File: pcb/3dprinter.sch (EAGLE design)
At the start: 1 part

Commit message: Footprint of TMC2100 and reference schematic added
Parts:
- added C1, C2, C4, C5, C6: 100n, 3dprinter:C-EUC0603
- added C3: 1u, 3dprinter:C-EUC0603
- added C7: 470n, 3dprinter:C-EUC0603
- added C8: 4.7u, 3dprinter:C-EUC0603
- added IC1: TMC2100, 3dprinter:TMC2100
- added PI_HEADER: (no value), 3dprinter:MA20-2
- added R1, R2: TBD, 3dprinter:R-US_R0805
- added R3: TBD, 3dprinter:R-US_R0603
- added R4: 2R2 / 3R3, 3dprinter:R-US_R0603
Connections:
- new net +12V: C1.2, C2.2, C3.2, C4.2, IC1.VS, IC1.VSA
- new net +5V: C6.1, IC1.VCC_IO
- new net 5V_M1: C8.1, IC1.5VOUT, R3.2, R4.2
- new net BRA_M1: IC1.BRA, R2.2
- new net BRB_M1: IC1.BRB, R1.2
- new net CFG1_M1: IC1.CFG1
- new net CFG2_M1: IC1.CFG2
- new net CPI_M1: C5.1, IC1.CPI
- new net CPO_M1: C5.2, IC1.CPO
- new net DIR_M1: IC1.DIR
- new net EN_M1: IC1.CFG6_!ENABLE
- new net GND: C1.1, C2.1, C3.1, C6.2, C7.2, C8.2, IC1.CFG0, IC1.CLK, IC1.GNDA, IC1.GNDD, IC1.GNDP, IC1.N.C, IC1.PAD, IC1.TST_MODE, R1.1, R2.1
- new net IREF_M1: IC1.AIN_IREF, R3.1
- new net OA1_M1: IC1.OA1
- new net OA2_M1: IC1.OA2
- new net OB1_M1: IC1.OB1
- new net OB2_M1: IC1.OB2
- new net PI_3V31: PI_HEADER.1
- new net STEP_M1: IC1.STEP
- new net VCC_M1: C7.1, IC1.VCC, R4.1
- new net VCP_M1: C4.1, IC1.VCP
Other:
- note added: "Raspberry Pi Header"
- note added: "TESTPOINT HERE"
- note added: "TODO: Trimpot Calculate I sense calculations Thermal pad on BOT? CFG table in schematic"
- note added: "TRIMPOT HERE"

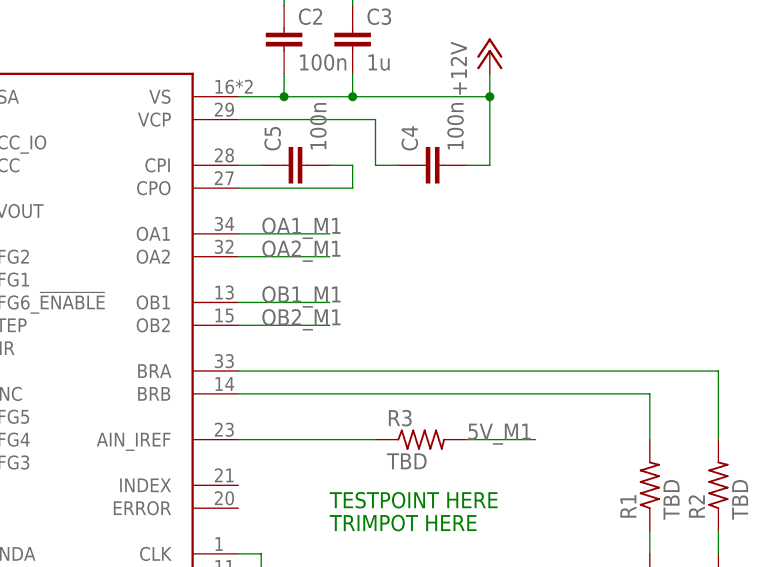
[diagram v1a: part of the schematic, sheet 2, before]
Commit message: TMC2100 initial routing
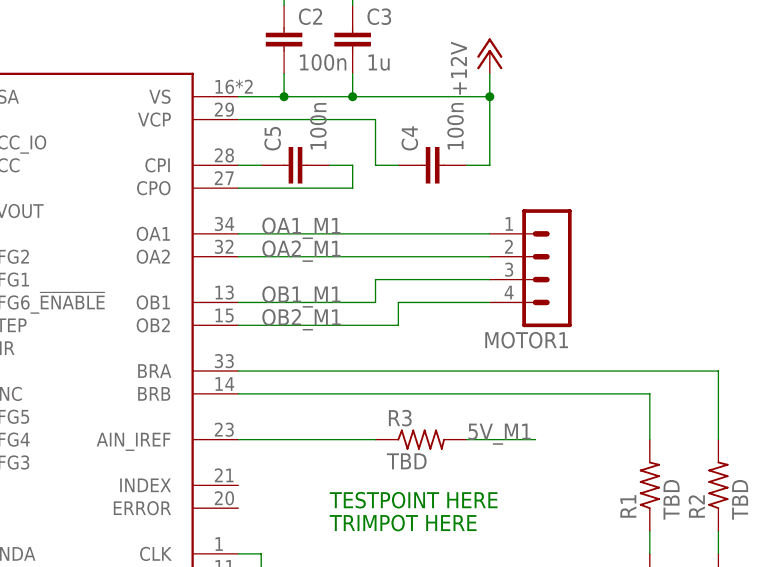
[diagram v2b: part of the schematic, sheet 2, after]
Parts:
- added MOTOR1: (no value), 3dprinter:MA04-1
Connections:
- net OA1_M1: now also MOTOR1.1
- net OA2_M1: now also MOTOR1.2
- net OB1_M1: now also MOTOR1.3
- net OB2_M1: now also MOTOR1.4
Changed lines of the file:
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@@
 <setting verticaltext="up"/>
 </settings>
-<grid distance="0.1" unitdist="inch" unit="inch" style="lines" multiple="1" display="yes" altdistance="0.01" altunitdist="inch" altunit="inch"/>
+<grid distance="0.1" unitdist="inch" unit="inch" style="lines" multiple="1" display="no" altdistance="0.01" altunitdist="inch" altunit="inch"/>
 <layers>
 <layer number="1" name="Top" color="4" fill="1" visible="no" active="no"/>
@@
 <part name="C8" library="3dprinter" deviceset="C-EU" device="C0603" value="4.7u"/>
 <part name="COPå8" library="supply" deviceset="GND" device=""/>
+<part name="MOTOR1" library="3dprinter" deviceset="MA04-1" device=""/>
 </parts>
 <sheets>
@@
 <instance part="C8" gate="G$1" x="45.72" y="208.28"/>
 <instance part="COPå8" gate="1" x="45.72" y="198.12"/>
+<instance part="MOTOR1" gate="1" x="139.7" y="205.74" rot="R180"/>
 </instances>
 <busses>
@@
 <segment>
 <pinref part="IC1" gate="G$1" pin="OA1"/>
-<wire x1="104.14" y1="210.82" x2="114.3" y2="210.82" width="0.1524" layer="91"/>
 <label x="106.68" y="210.82" size="1.778" layer="95"/>
+<wire x1="104.14" y1="210.82" x2="132.08" y2="210.82" width="0.1524" layer="91"/>
+<pinref part="MOTOR1" gate="1" pin="1"/>
 </segment>
 </net>
@@
 <segment>
 <pinref part="IC1" gate="G$1" pin="OA2"/>
-<wire x1="104.14" y1="208.28" x2="114.3" y2="208.28" width="0.1524" layer="91"/>
 <label x="106.68" y="208.28" size="1.778" layer="95"/>
+<wire x1="104.14" y1="208.28" x2="132.08" y2="208.28" width="0.1524" layer="91"/>
+<pinref part="MOTOR1" gate="1" pin="2"/>
 </segment>
 </net>
@@
 <segment>
 <pinref part="IC1" gate="G$1" pin="OB1"/>
-<wire x1="104.14" y1="203.2" x2="114.3" y2="203.2" width="0.1524" layer="91"/>
+<wire x1="104.14" y1="203.2" x2="119.38" y2="203.2" width="0.1524" layer="91"/>
 <label x="106.68" y="203.2" size="1.778" layer="95"/>
+<wire x1="119.38" y1="203.2" x2="119.38" y2="205.74" width="0.1524" layer="91"/>
+<wire x1="119.38" y1="205.74" x2="132.08" y2="205.74" width="0.1524" layer="91"/>
+<pinref part="MOTOR1" gate="1" pin="3"/>
 </segment>
 </net>
@@
 <segment>
 <pinref part="IC1" gate="G$1" pin="OB2"/>
-<wire x1="104.14" y1="200.66" x2="114.3" y2="200.66" width="0.1524" layer="91"/>
+<wire x1="104.14" y1="200.66" x2="121.92" y2="200.66" width="0.1524" layer="91"/>
 <label x="106.68" y="200.66" size="1.778" layer="95"/>
-</segment>
-</net>
+<wire x1="121.92" y1="200.66" x2="121.92" y2="203.2" width="0.1524" layer="91"/>
+<wire x1="121.92" y1="203.2" x2="132.08" y2="203.2" width="0.1524" layer="91"/>
+<pinref part="MOTOR1" gate="1" pin="4"/>
+</segment>
+</net>

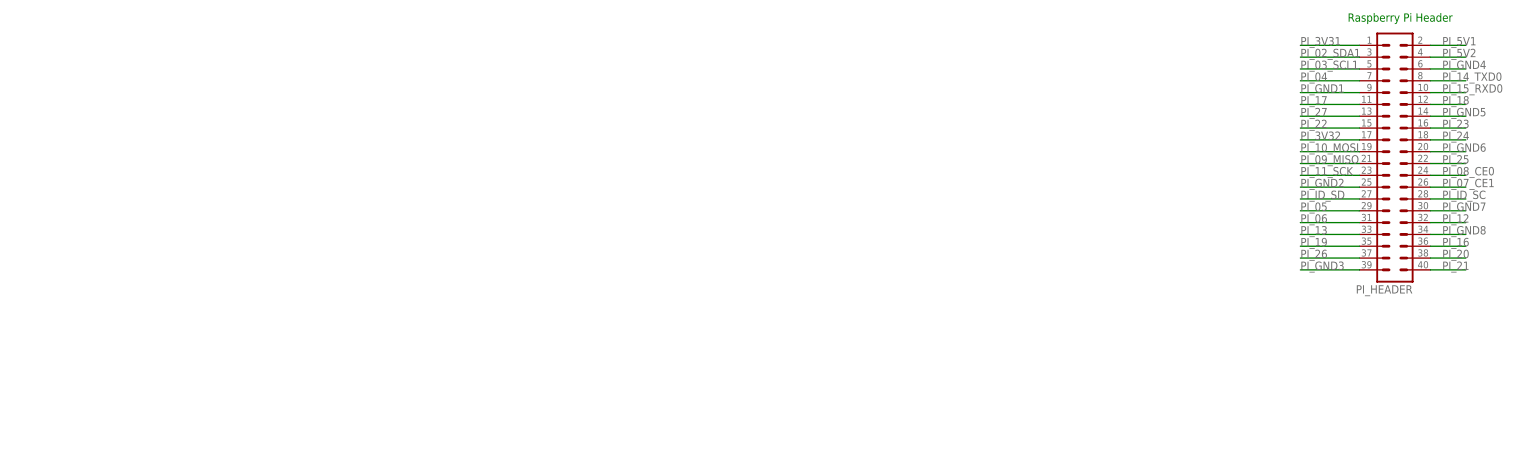
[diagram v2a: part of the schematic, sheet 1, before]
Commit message: Added NRF51822 footprint
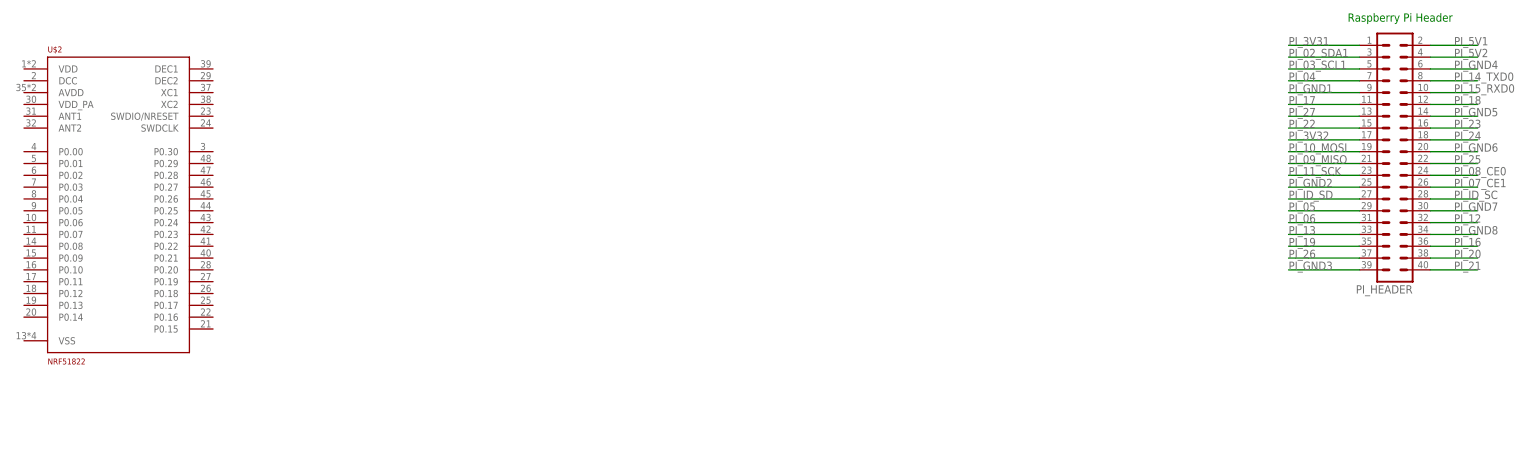
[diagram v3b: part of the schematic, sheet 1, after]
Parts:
- added U$2: NRF51822, 3dprinter:NRF51822
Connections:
- new net PI_02_SDA1: PI_HEADER.3
- new net PI_03_SCL1: PI_HEADER.5
- new net PI_04: PI_HEADER.7
- new net PI_05: PI_HEADER.29
- new net PI_06: PI_HEADER.31
- new net PI_07_CE1: PI_HEADER.26
- new net PI_08_CE0: PI_HEADER.24
- new net PI_09_MISO: PI_HEADER.21
- new net PI_10_MOSI: PI_HEADER.19
- new net PI_11_SCK: PI_HEADER.23
- new net PI_12: PI_HEADER.32
- new net PI_13: PI_HEADER.33
- new net PI_14_TXD0: PI_HEADER.8
- new net PI_15_RXD0: PI_HEADER.10
- new net PI_16: PI_HEADER.36
- new net PI_17: PI_HEADER.11
- new net PI_18: PI_HEADER.12
- new net PI_19: PI_HEADER.35
- new net PI_20: PI_HEADER.38
- new net PI_21: PI_HEADER.40
- new net PI_22: PI_HEADER.15
- new net PI_23: PI_HEADER.16
- new net PI_24: PI_HEADER.18
- new net PI_25: PI_HEADER.22
- new net PI_26: PI_HEADER.37
- new net PI_27: PI_HEADER.13
- new net PI_3V32: PI_HEADER.17
- new net PI_5V1: PI_HEADER.2
- new net PI_5V2: PI_HEADER.4
- new net PI_GND1: PI_HEADER.9
- new net PI_GND2: PI_HEADER.25
- new net PI_GND3: PI_HEADER.39
- new net PI_GND4: PI_HEADER.6
- new net PI_GND5: PI_HEADER.14
- new net PI_GND6: PI_HEADER.20
- new net PI_GND7: PI_HEADER.30
- new net PI_GND8: PI_HEADER.34
- new net PI_ID_SC: PI_HEADER.28
- new net PI_ID_SD: PI_HEADER.27
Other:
- moved on the sheet: IC1

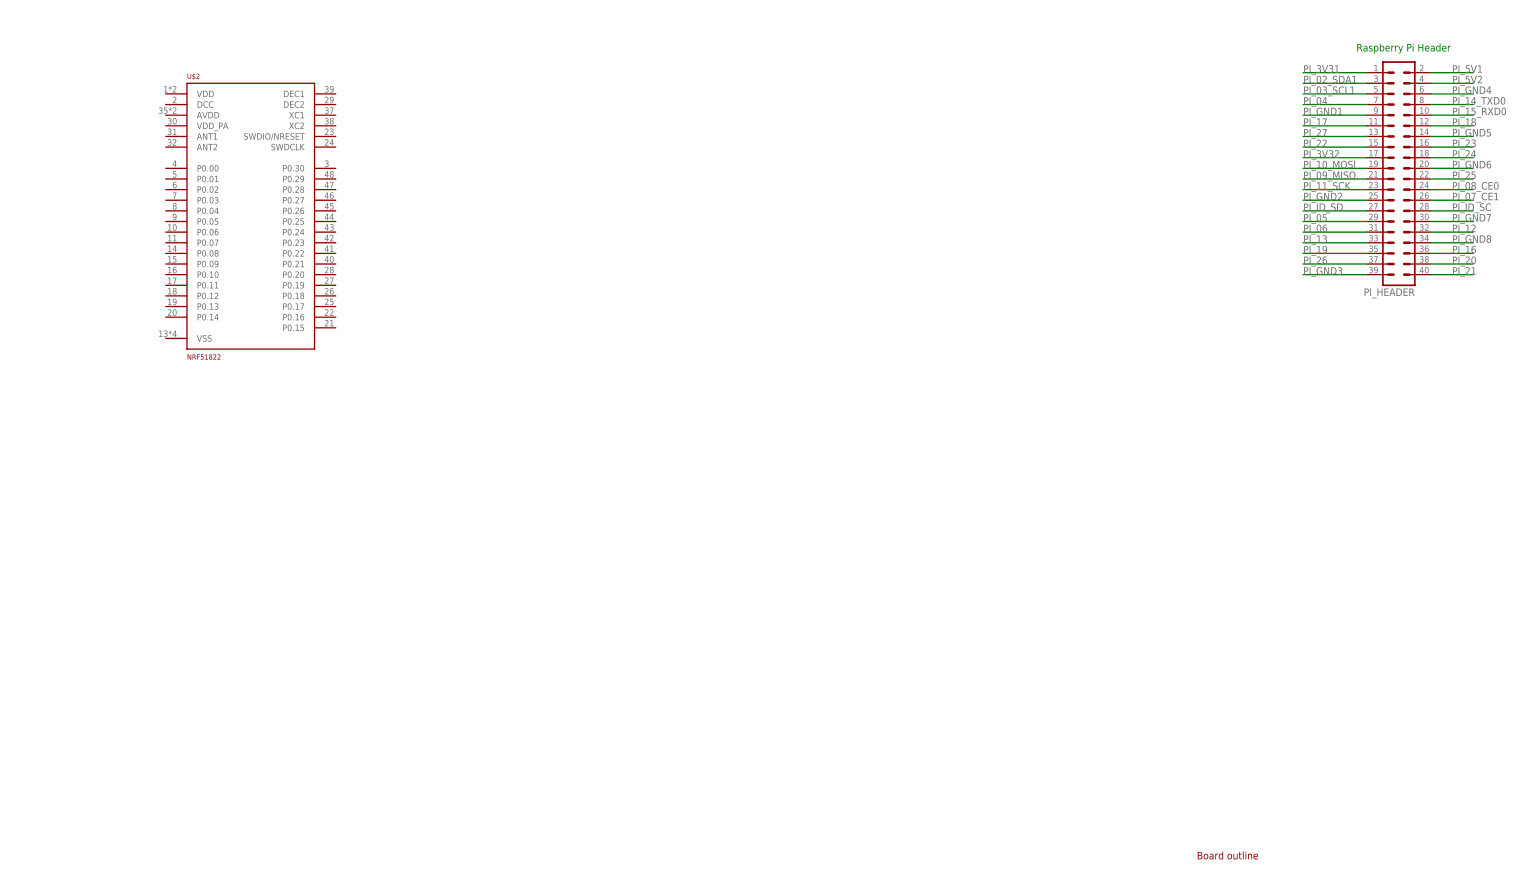
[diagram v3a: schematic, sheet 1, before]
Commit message: Example circuit nrf51 passives
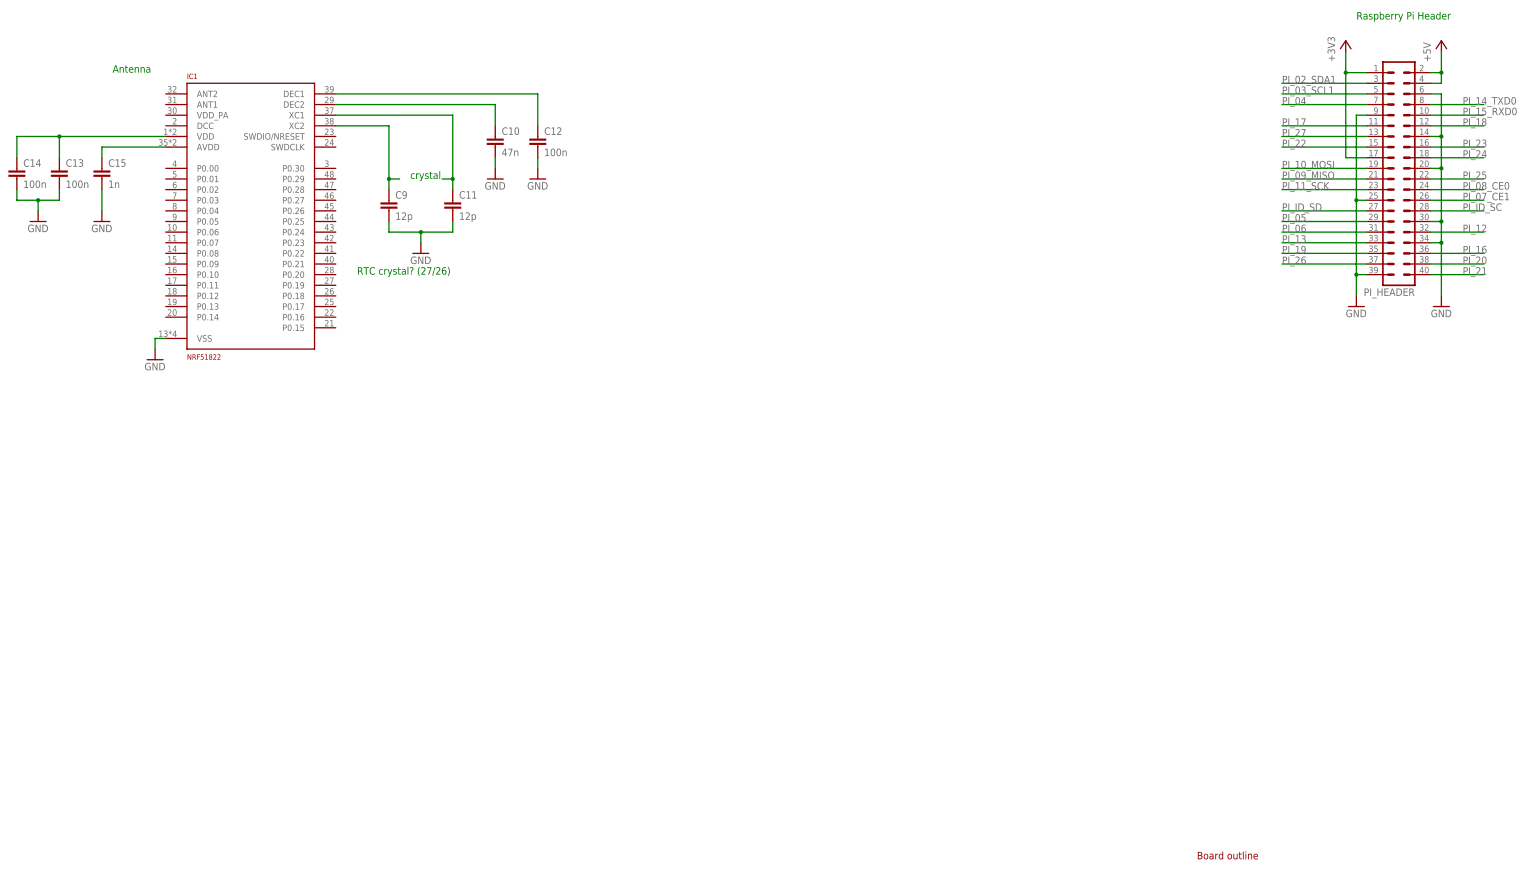
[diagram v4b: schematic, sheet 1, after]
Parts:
- removed U$2: NRF51822, 3dprinter:NRF51822
- added C10: 47n, 3dprinter:C-EUC0603
- added C11, C9: 12p, 3dprinter:C-EUC0603
- added C12, C13, C14: 100n, 3dprinter:C-EUC0603
- added C15: 1n, 3dprinter:C-EUC0603
- added IC2: TMC2100, 3dprinter:TMC2100
- IC1: value TMC2100 -> NRF51822; device 3dprinter:TMC2100 -> 3dprinter:NRF51822
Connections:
- removed net PI_3V31: PI_HEADER.1
- removed net PI_3V32: PI_HEADER.17
- removed net PI_5V1: PI_HEADER.2
- removed net PI_5V2: PI_HEADER.4
- removed net PI_GND1: PI_HEADER.9
- removed net PI_GND2: PI_HEADER.25
- removed net PI_GND3: PI_HEADER.39
- removed net PI_GND4: PI_HEADER.6
- removed net PI_GND5: PI_HEADER.14
- removed net PI_GND6: PI_HEADER.20
- removed net PI_GND7: PI_HEADER.30
- removed net PI_GND8: PI_HEADER.34
- new net +3V3: PI_HEADER.1, PI_HEADER.17
- new net N$1: C9.1, IC1.XC2
- new net N$2: C11.1, IC1.XC1
- new net N$3: C12.1, IC1.DEC1
- new net N$4: C10.1, IC1.DEC2
- new net N$5: C13.1, C14.1, IC1.VDD
- new net N$6: C15.1, IC1.AVDD
- net +12V: now also IC2.VS, IC2.VSA; no longer IC1.VS, IC1.VSA
- net +5V: now also IC2.VCC_IO, PI_HEADER.2, PI_HEADER.4; no longer IC1.VCC_IO
- net 5V_M1: now also IC2.5VOUT; no longer IC1.5VOUT
- net BRA_M1: now also IC2.BRA; no longer IC1.BRA
- net BRB_M1: now also IC2.BRB; no longer IC1.BRB
- net CFG1_M1: now also IC2.CFG1; no longer IC1.CFG1
- net CFG2_M1: now also IC2.CFG2; no longer IC1.CFG2
- net CPI_M1: now also IC2.CPI; no longer IC1.CPI
- net CPO_M1: now also IC2.CPO; no longer IC1.CPO
- net DIR_M1: now also IC2.DIR; no longer IC1.DIR
- net EN_M1: now also IC2.CFG6_!ENABLE; no longer IC1.CFG6_!ENABLE
- net GND: now also C10.2, C11.2, C12.2, C13.2, C14.2, C15.2, C9.2, IC1.VSS, IC2.CFG0, IC2.CLK, IC2.GNDA, IC2.GNDD, IC2.GNDP, IC2.N.C, IC2.PAD, IC2.TST_MODE, PI_HEADER.14, PI_HEADER.20, PI_HEADER.25, PI_HEADER.30, PI_HEADER.34, PI_HEADER.39, PI_HEADER.6, PI_HEADER.9; no longer IC1.CFG0, IC1.CLK, IC1.GNDA, IC1.GNDD, IC1.GNDP, IC1.N.C, IC1.PAD, IC1.TST_MODE
- net IREF_M1: now also IC2.AIN_IREF; no longer IC1.AIN_IREF
- net OA1_M1: now also IC2.OA1; no longer IC1.OA1
- net OA2_M1: now also IC2.OA2; no longer IC1.OA2
- net OB1_M1: now also IC2.OB1; no longer IC1.OB1
- net OB2_M1: now also IC2.OB2; no longer IC1.OB2
- net STEP_M1: now also IC2.STEP; no longer IC1.STEP
- net VCC_M1: now also IC2.VCC; no longer IC1.VCC
- net VCP_M1: now also IC2.VCP; no longer IC1.VCP
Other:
- note added: "Antenna"
- note added: "RTC crystal? (27/26)"
- note added: "crystal"

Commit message: Multiplied motor driver circuit and added mosfets
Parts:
- added ANT: ANTENNA, 3dprinter:ANTENNA
- added BAL: BALUNBALUN, 3dprinter:BALUNBALUN
- added C1_M1, C1_M2, C1_M3, C1_M4, C2_M2, C2_M3, C2_M4, C4_M2, C4_M3, C4_M4, C5_M2, C5_M3, C5_M4, C6_M2, C6_M3, C6_M4: 100n, 3dprinter:C-EUC0603
- added C3_M2, C3_M3, C3_M4: 1u, 3dprinter:C-EUC0603
- added C7_M2, C7_M3, C7_M4: 470n, 3dprinter:C-EUC0603
- added C8_M2, C8_M3, C8_M4: 4.7u, 3dprinter:C-EUC0603
- added IC_M2, IC_M3, IC_M4: TMC2100, 3dprinter:TMC2100
- added MOTOR2, MOTOR3, MOTOR4, SWD: (no value), 3dprinter:MA04-1
- added POT_M1, POT_M2, POT_M3, POT_M4: TRIMPOT, 3dprinter:TRIMPOT
- added Q1, Q2, Q3, Q4: MOSFET, 3dprinter:MOSFET
- added R1_M2, R1_M3, R1_M4: 20k, 3dprinter:R-US_R0603
- added R2_M2, R2_M3, R2_M4, R3_M2, R3_M3, R3_M4: TBD, 3dprinter:R-US_R0805
- added R4_M2, R4_M3, R4_M4: 2R2 / 3R3, 3dprinter:R-US_R0603
- added Y1: CRYSTAL, 3dprinter:CRYSTAL
- C1: value 100n -> 2.2n
- R1_M1: value TBD -> 20k
- renumbered C2 to C2_M1, C3 to C3_M1, C4 to C4_M1, C5 to C5_M1, C6 to C6_M1, C7 to C7_M1, C8 to C8_M1, IC2 to IC_M1, R1 to R2_M1, R2 to R3_M1, R3 to R1_M1, R4 to R4_M1, U$1 to OUTLINE
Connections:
- removed net IREF_M1: IC_M1.AIN_IREF, R1_M1.1
- new net 5V_M2: C8_M2.1, IC_M2.5VOUT, R1_M2.2, R4_M2.2
- new net 5V_M3: C8_M3.1, IC_M3.5VOUT, R1_M3.2, R4_M3.2
- new net 5V_M4: C8_M4.1, IC_M4.5VOUT, R1_M4.2, R4_M4.2
- new net AIN_M1: IC_M1.AIN_IREF, POT_M1.2
- new net AIN_M2: IC_M2.AIN_IREF, POT_M2.2
- new net AIN_M3: IC_M3.AIN_IREF, POT_M3.2
- new net AIN_M4: IC_M4.AIN_IREF, POT_M4.2
- new net BRA_M2: IC_M2.BRA, R3_M2.2
- new net BRA_M3: IC_M3.BRA, R3_M3.2
- new net BRA_M4: IC_M4.BRA, R3_M4.2
- new net BRB_M2: IC_M2.BRB, R2_M2.2
- new net BRB_M3: IC_M3.BRB, R2_M3.2
- new net BRB_M4: IC_M4.BRB, R2_M4.2
- new net CFG1_M2: IC_M2.CFG1
- new net CFG1_M3: IC_M3.CFG1
- new net CFG1_M4: IC_M4.CFG1
- new net CFG2_M2: IC_M2.CFG2
- new net CFG2_M3: IC_M3.CFG2
- new net CFG2_M4: IC_M4.CFG2
- new net CPI_M2: C5_M2.1, IC_M2.CPI
- new net CPI_M3: C5_M3.1, IC_M3.CPI
- new net CPI_M4: C5_M4.1, IC_M4.CPI
- new net CPO_M2: C5_M2.2, IC_M2.CPO
- new net CPO_M3: C5_M3.2, IC_M3.CPO
- new net CPO_M4: C5_M4.2, IC_M4.CPO
- new net DIR_M2: IC_M2.DIR
- new net DIR_M3: IC_M3.DIR
- new net DIR_M4: IC_M4.DIR
- new net EN_M2: IC_M2.CFG6_!ENABLE
- new net EN_M3: IC_M3.CFG6_!ENABLE
- new net EN_M4: IC_M4.CFG6_!ENABLE
- new net N$10: BAL.BAL2, IC1.ANT2
- new net N$7: ANT.1, BAL.UBAL
- new net N$8: BAL.DC, C1.1, IC1.VDD_PA
- new net N$9: BAL.BAL1, IC1.ANT1
- new net OA1_M2: IC_M2.OA1, MOTOR2.1
- new net OA1_M3: IC_M3.OA1, MOTOR3.1
- new net OA1_M4: IC_M4.OA1, MOTOR4.1
- new net OA2_M2: IC_M2.OA2, MOTOR2.2
- new net OA2_M3: IC_M3.OA2, MOTOR3.2
- new net OA2_M4: IC_M4.OA2, MOTOR4.2
- new net OB1_M2: IC_M2.OB1, MOTOR2.3
- new net OB1_M3: IC_M3.OB1, MOTOR3.3
- new net OB1_M4: IC_M4.OB1, MOTOR4.3
- new net OB2_M2: IC_M2.OB2, MOTOR2.4
- new net OB2_M3: IC_M3.OB2, MOTOR3.4
- new net OB2_M4: IC_M4.OB2, MOTOR4.4
- new net POT_M1: POT_M1.1, R1_M1.1
- new net POT_M2: POT_M2.1, R1_M2.1
- new net POT_M3: POT_M3.1, R1_M3.1
- new net POT_M4: POT_M4.1, R1_M4.1
- new net STEP_M2: IC_M2.STEP
- new net STEP_M3: IC_M3.STEP
- new net STEP_M4: IC_M4.STEP
- new net SWDCLK: IC1.SWDCLK, SWD.2
- new net SWDIO: IC1.SWDIO/NRESET, SWD.3
- new net VCC_M2: C7_M2.1, IC_M2.VCC, R4_M2.1
- new net VCC_M3: C7_M3.1, IC_M3.VCC, R4_M3.1
- new net VCC_M4: C7_M4.1, IC_M4.VCC, R4_M4.1
- new net VCP_M2: C4_M2.1, IC_M2.VCP
- new net VCP_M3: C4_M3.1, IC_M3.VCP
- new net VCP_M4: C4_M4.1, IC_M4.VCP
- net +12V: now also C1_M1.2, C1_M2.2, C1_M3.2, C1_M4.2, C2_M2.2, C2_M3.2, C2_M4.2, C3_M2.2, C3_M3.2, C3_M4.2, C4_M2.2, C4_M3.2, C4_M4.2, IC_M2.VS, IC_M2.VSA, IC_M3.VS, IC_M3.VSA, IC_M4.VS, IC_M4.VSA; no longer C1.2
- net +3V3: now also C13.1, C14.1, IC1.VDD; no longer PI_HEADER.1, PI_HEADER.17
- net +5V: now also C6_M2.1, C6_M3.1, C6_M4.1, IC_M2.VCC_IO, IC_M3.VCC_IO, IC_M4.VCC_IO
- net GND: now also BAL.GND, C1.2, C1_M1.1, C1_M2.1, C1_M3.1, C1_M4.1, C2_M2.1, C2_M3.1, C2_M4.1, C3_M2.1, C3_M3.1, C3_M4.1, C6_M2.2, C6_M3.2, C6_M4.2, C7_M2.2, C7_M3.2, C7_M4.2, C8_M2.2, C8_M3.2, C8_M4.2, IC_M2.CFG0, IC_M2.CLK, IC_M2.GNDA, IC_M2.GNDD, IC_M2.GNDP, IC_M2.N.C, IC_M2.PAD, IC_M2.TST_MODE, IC_M3.CFG0, IC_M3.CLK, IC_M3.GNDA, IC_M3.GNDD, IC_M3.GNDP, IC_M3.N.C, IC_M3.PAD, IC_M3.TST_MODE, IC_M4.CFG0, IC_M4.CLK, IC_M4.GNDA, IC_M4.GNDD, IC_M4.GNDP, IC_M4.N.C, IC_M4.PAD, IC_M4.TST_MODE, POT_M1.3, POT_M2.3, POT_M3.3, POT_M4.3, R2_M2.1, R2_M3.1, R2_M4.1, R3_M2.1, R3_M3.1, R3_M4.1, SWD.1, Y1.2; no longer C1.1
- net N$1: now also Y1.1
- net N$2: now also Y1.3
- net N$5: now also PI_HEADER.1, PI_HEADER.17; no longer C13.1, C14.1, IC1.VDD
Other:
- note added: "3v3"
- note added: "TODO: Calculate I sense calculations Thermal pad on BOT? CFG table in schematic"
- note added: "TODO: change fan mosfets to smaller ones"
- note removed: "Antenna"
- note removed: "RTC crystal? (27/26)"
- note removed: "TESTPOINT HERE"
- note removed: "TODO: Trimpot Calculate I sense calculations Thermal pad on BOT? CFG table in schematic"
- note removed: "TRIMPOT HERE"
- note removed: "crystal"
